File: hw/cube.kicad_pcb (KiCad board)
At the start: 4 copper layers, 48 x 52 mm, 63 parts, among them J1 USB-C, J2 ECRAN QSPI, J3 microSD, J4 HP, J5 I2C EXT, J6 DEBUG, SW1 RESET, SW2 BOOT, U1 AP63203WU, U2 ESP32-S3-WROOM-1U-N16R8, U3 MAX98357A, U4 VL53L1X, U5 LIS3DH

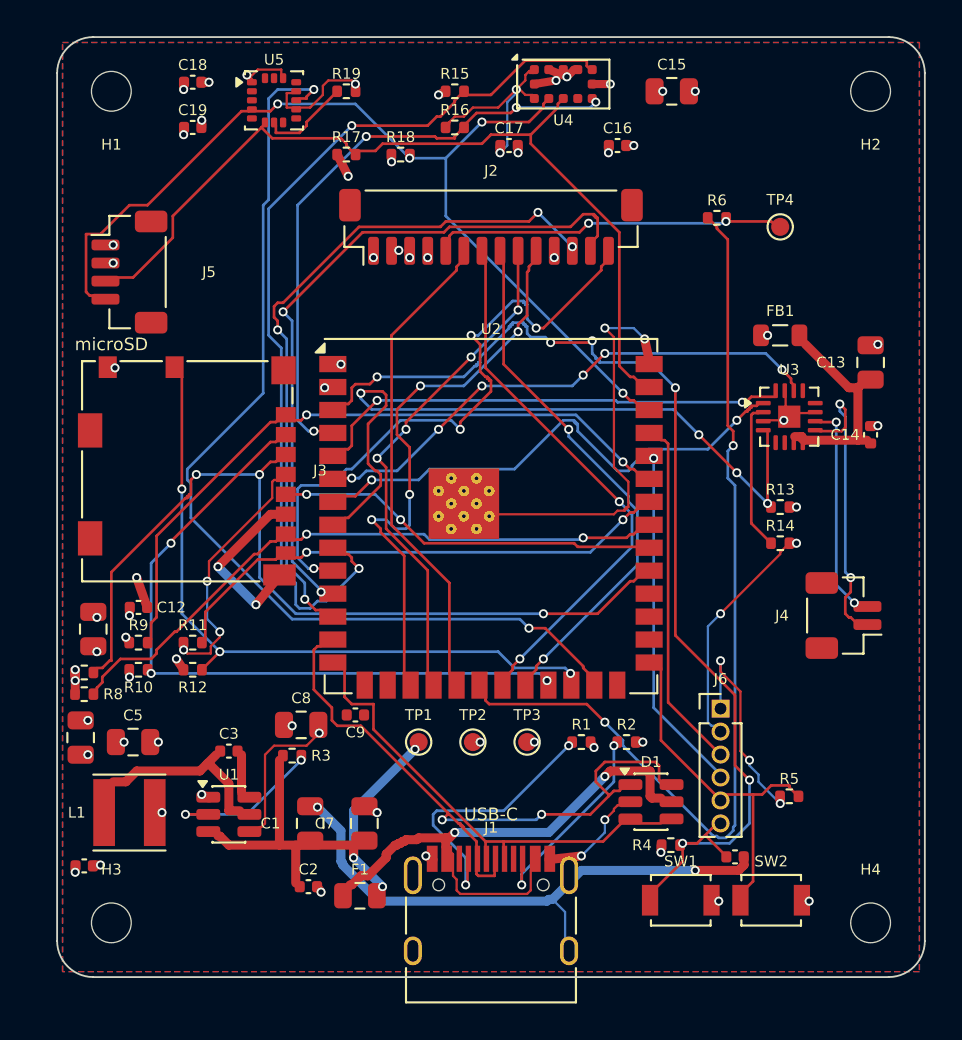
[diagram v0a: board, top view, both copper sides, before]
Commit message: feat(hw): carte entierement routee — 223/223 connexions
Les 4 dernieres liaisons, autour du LIS3DH (LGA-16 au pas de 0,5 mm), ont ete
tirees a la main dans Pcbnew. La masse de U5 passe par une piste sur In2.Cu et
un via vers le plan : cela cree une fente courte dans le plan +3V3, dans un
coin qui ne consomme que des microamperes, donc sans consequence.

tools/import_routes.py recapture ce cuivre dans routes.json : le routage
manuel fait desormais partie du pipeline au lieu d'etre perdu a la prochaine
generation. Le format accepte un nom de couche et la taille reelle des vias,
ce qu'exigeaient la piste sur couche interne et les vias 0,7/0,35.

Corrections associees, toutes signalees par le DRC :
- serigraphie remontee de 0,6 a 0,8 mm : sous 0,8 mm le texte n'est pas
  garanti lisible par le fabricant (75 avertissements) ;
- H1-H4 et TP1-TP4 declares hors nomenclature cote schema, les empreintes
  portaient deja le drapeau (8 divergences empreinte/symbole) ;
- deux moignons de 0,1 mm sur USB_DM supprimes.

Etat : 0 erreur ERC, 0 violation DRC, 0 liaison non routee, 0 ecart de parite.
Restent 8 avertissements de serigraphie cosmetiques.
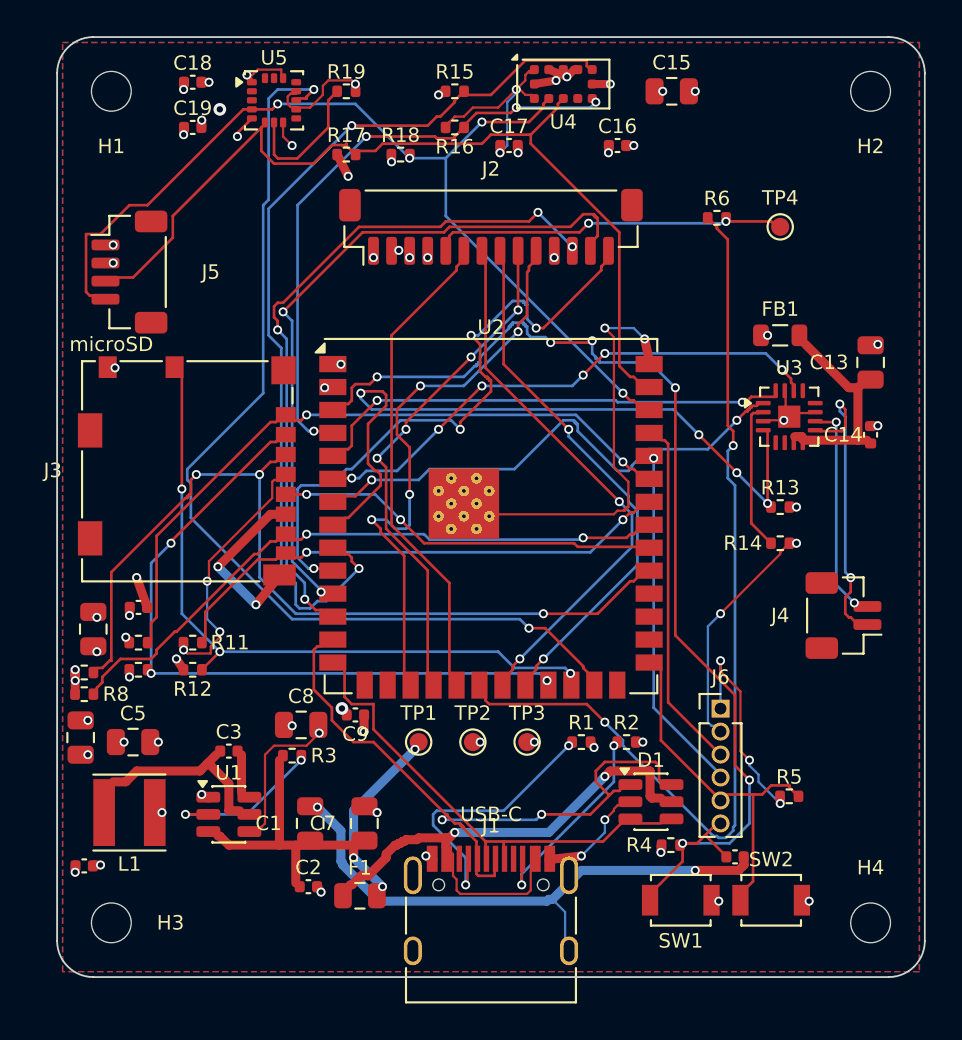
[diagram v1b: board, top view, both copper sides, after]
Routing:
- net GND: track 116.1 -> 120.4 mm, vias 43 -> 46
- net /ACC_ADDR: track 4.59 -> 7.50 mm
- net +3V3: track 53.0 -> 55.0 mm, vias 36 -> 38
- net /I2C_SDA: track 46.9 -> 48.6 mm
